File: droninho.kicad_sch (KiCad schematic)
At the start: 22 parts, among them J1 Conn_01x02_Pin, J2 M2, J3 M1, J4 M3, J5 M4, J6 I2C, J7 TXD0/RXD0, J8 I2C, Q1 SI2300, Q2 SI2300, Q3 SI2300, Q4 SI2300, U2 ESP32 Dev Kit, U4 MPU9250/6500

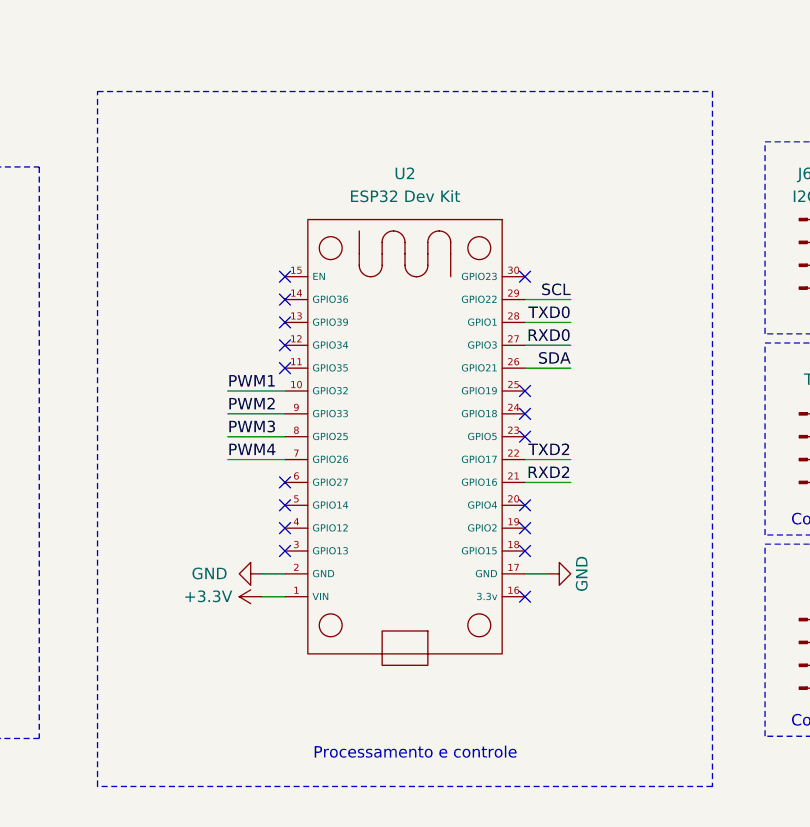
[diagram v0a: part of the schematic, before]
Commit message: Versão com WIFI de fora da placa.
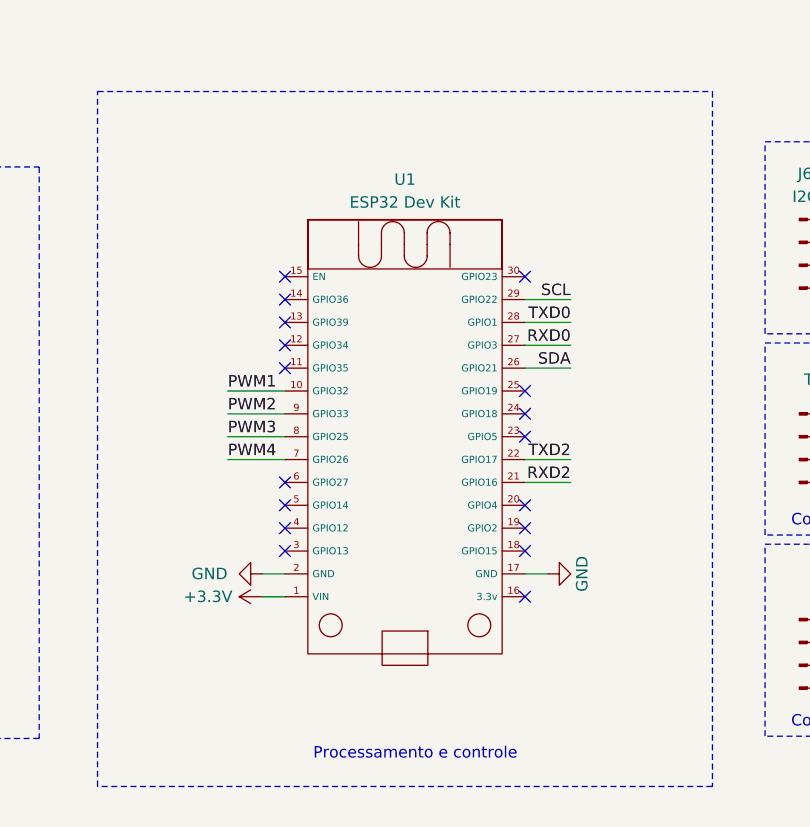
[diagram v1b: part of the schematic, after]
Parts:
- removed U2: ESP32 Dev Kit, Library:ESP32_30pin, symbol Library:ESP32_30Pin
- added U1: ESP32 Dev Kit, Library:ESP32_30pin vertical WIFI, symbol Library:ESP32_30Pin_vertical_WIFI
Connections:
- net +3.3V: now also U1.1 (VIN)
- net GND: now also U1.17 (GND), U1.2 (GND)
- net PWM1: now also U1.10 (GPIO32)
- net PWM2: now also U1.9 (GPIO33)
- net PWM3: now also U1.8 (GPIO25)
- net PWM4: now also U1.7 (GPIO26)
- net RXD0: now also U1.27 (GPIO3)
- net RXD2: now also U1.21 (GPIO16)
- net SCL: now also U1.29 (GPIO22)
- net SDA: now also U1.26 (GPIO21)
- net TXD0: now also U1.28 (GPIO1)
- net TXD2: now also U1.22 (GPIO17)
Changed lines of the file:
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@@
+	)
+	(symbol
+		(lib_id "Library:ESP32_30Pin_vertical_WIFI")
+		(at 207.01 95.885 0)
+		(unit 1)
+		(exclude_from_sim no)
+		(in_bom yes)
+		(on_board yes)
+		(dnp no)
+		(fields_autoplaced yes)
+		(property "Reference" "U1"
+			(at 206.375 70.485 0)
+			(effects
+				(font
+					(size 1.27 1.27)
+				)
+			)
+		)
+		(property "Value" "ESP32 Dev Kit"
+			(at 206.375 73.025 0)
+			(effects
+				(font
+					(size 1.27 1.27)
+				)
+			)
+		)
+		(property "Footprint" "Library:ESP32_30pin vertical WIFI"
+			(at 206.375 72.39 0)
+			(effects
+				(font
+					(size 1.27 1.27)
+					(color 194 194 0 1)
+				)
+				(hide yes)
+			)
+		)
+		(property "Datasheet" ""
+			(at 207.01 95.885 0)
+			(effects
+				(font
+					(size 1.27 1.27)
+				)
+				(hide yes)
+			)
+		)
+		(property "Description" ""
+			(at 207.01 95.885 0)
+			(effects
+				(font
+					(size 1.27 1.27)
+				)
+				(hide yes)
+			)
+		)
+		(pin "2"
+		)
+		(pin "24"
+		)
+		(pin "23"
+		)
+		(pin "6"
+		)
+		(pin "19"
+		)
+		(pin "11"
+		)
+		(pin "16"
+		)
+		(pin "14"
+		)
+		(pin "15"
+		)
+		(pin "5"
+		)
+		(pin "7"
+		)
+		(pin "10"
+		)
+		(pin "1"
+		)
+		(pin "8"
+		)
+		(pin "3"
+		)
+		(pin "28"
+		)
+		(pin "12"
+		)
+		(pin "4"
+		)
+		(pin "27"
+		)
+		(pin "13"
+		)
+		(pin "9"
+		)
+		(pin "30"
+		)
+		(pin "29"
+		)
+		(pin "26"
+		)
+		(pin "25"
+		)
+		(pin "22"
+		)
+		(pin "21"
+		)
+		(pin "20"
+		)
+		(pin "18"
+		)
+		(pin "17"
+		)
+		(instances
+			(project ""
+				(path "/50215636-8ce2-4b01-ade7-3715bffabe9d"
+					(reference "U1")
+					(unit 1)
+				)
+			)
+		)
 	)
 	(symbol
@@
 					(unit 1)
 				)
-			)
-		)
-	)
-	(symbol
-		(lib_id "Library:ESP32_30Pin")
-		(at 206.375 99.06 270)
-		(unit 1)
-		(exclude_from_sim no)
-		(in_bom yes)
-		(on_board yes)
-		(dnp no)
-		(fields_autoplaced yes)
-		(property "Reference" "U2"
-			(at 206.375 69.85 90)
-			(effects
-				(font
-					(size 1.27 1.27)
-				)
-			)
-		)
-		(property "Value" "ESP32 Dev Kit"
-			(at 206.375 72.39 90)
-			(effects
-				(font
-					(size 1.27 1.27)
-				)
-			)
-		)
-		(property "Footprint" "Library:ESP32_30pin"
-			(at 206.375 72.39 90)
-			(effects
-				(font
-					(size 1.27 1.27)
-					(color 194 194 0 1)
-				)
-				(hide yes)
-			)
-		)
-		(property "Datasheet" ""
-			(at 206.375 99.06 0)
-			(effects
-				(font
-					(size 1.27 1.27)
-				)
-				(hide yes)
-			)
-		)
-		(property "Description" ""
-			(at 206.375 99.06 0)
-			(effects
-				(font
-					(size 1.27 1.27)
-				)
-				(hide yes)
-			)
-		)
-		(pin "15"
-		)
-		(pin "14"
-		)
-		(pin "30"
-		)
-		(pin "29"
-		)
-		(pin "19"
-		)
-		(pin "7"
-		)
-		(pin "12"
-		)
-		(pin "21"
-		)
-		(pin "6"
-		)
-		(pin "9"
-		)
-		(pin "26"
-		)
-		(pin "24"
-		)
-		(pin "17"
-		)
-		(pin "5"
-		)
-		(pin "13"
-		)
-		(pin "10"
-		)
-		(pin "25"
-		)
-		(pin "23"
-		)
-		(pin "8"
-		)
-		(pin "22"
-		)
-		(pin "20"
-		)
-		(pin "28"
-		)
-		(pin "18"
-		)
-		(pin "3"
-		)
-		(pin "2"
-		)
-		(pin "11"
-		)
-		(pin "27"
-		)
-		(pin "4"
-		)
-		(pin "16"
-		)
-		(pin "1"
-		)
-		(instances
-			(project ""
-				(path "/50215636-8ce2-4b01-ade7-3715bffabe9d"
-					(reference "U2")
-					(unit 1)
-				)

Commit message: Correções em footprints e troca de lado do ESP32.
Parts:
- D1, D2, D3, D4: footprint Diode_SMD:D_SOD-110 -> Diode_SMD:D_SOD-123
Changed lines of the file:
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@@
 			)
 		)
-		(property "Footprint" "Diode_SMD:D_SOD-110"
+		(property "Footprint" "Diode_SMD:D_SOD-123"
 			(at 86.106 161.036 0)
 			(effects
@@
 			)
 		)
-		(property "Footprint" "Diode_SMD:D_SOD-110"
+		(property "Footprint" "Diode_SMD:D_SOD-123"
 			(at 86.106 116.586 0)
 			(effects
@@
 			)
 		)
-		(property "Footprint" "Diode_SMD:D_SOD-110"
+		(property "Footprint" "Diode_SMD:D_SOD-123"
 			(at 83.566 28.956 0)
 			(effects
@@
 			)
 		)
-		(property "Footprint" "Diode_SMD:D_SOD-110"
+		(property "Footprint" "Diode_SMD:D_SOD-123"
 			(at 83.566 72.136 0)
 			(effects

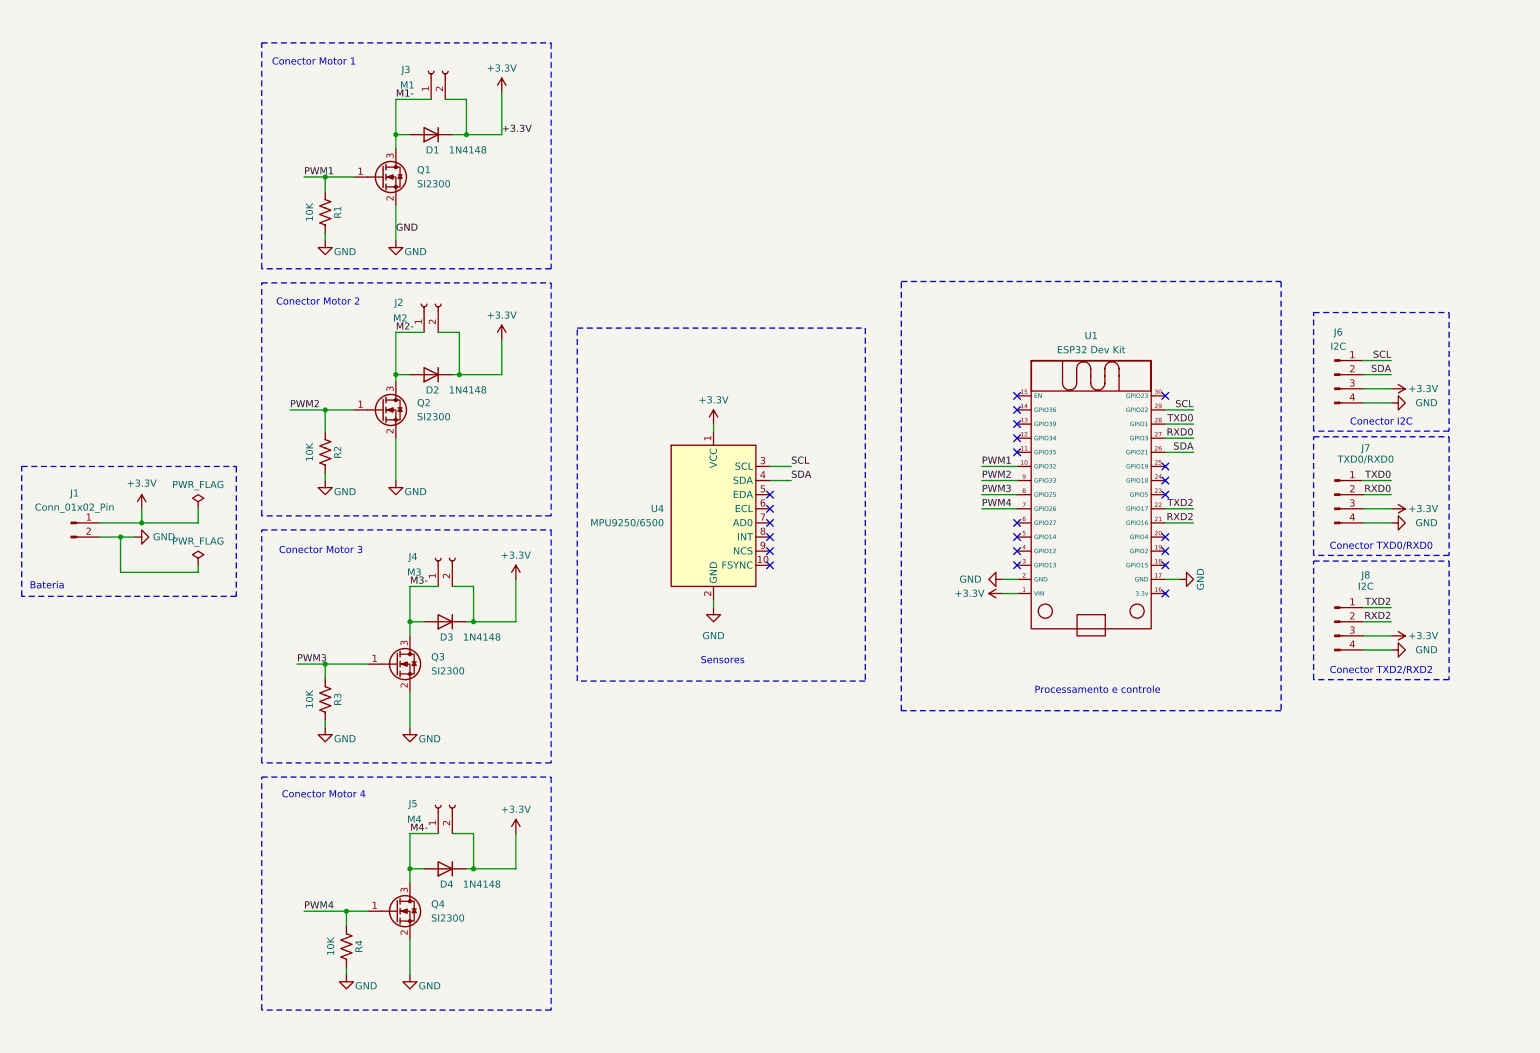
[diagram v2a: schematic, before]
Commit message: voltage regulator added
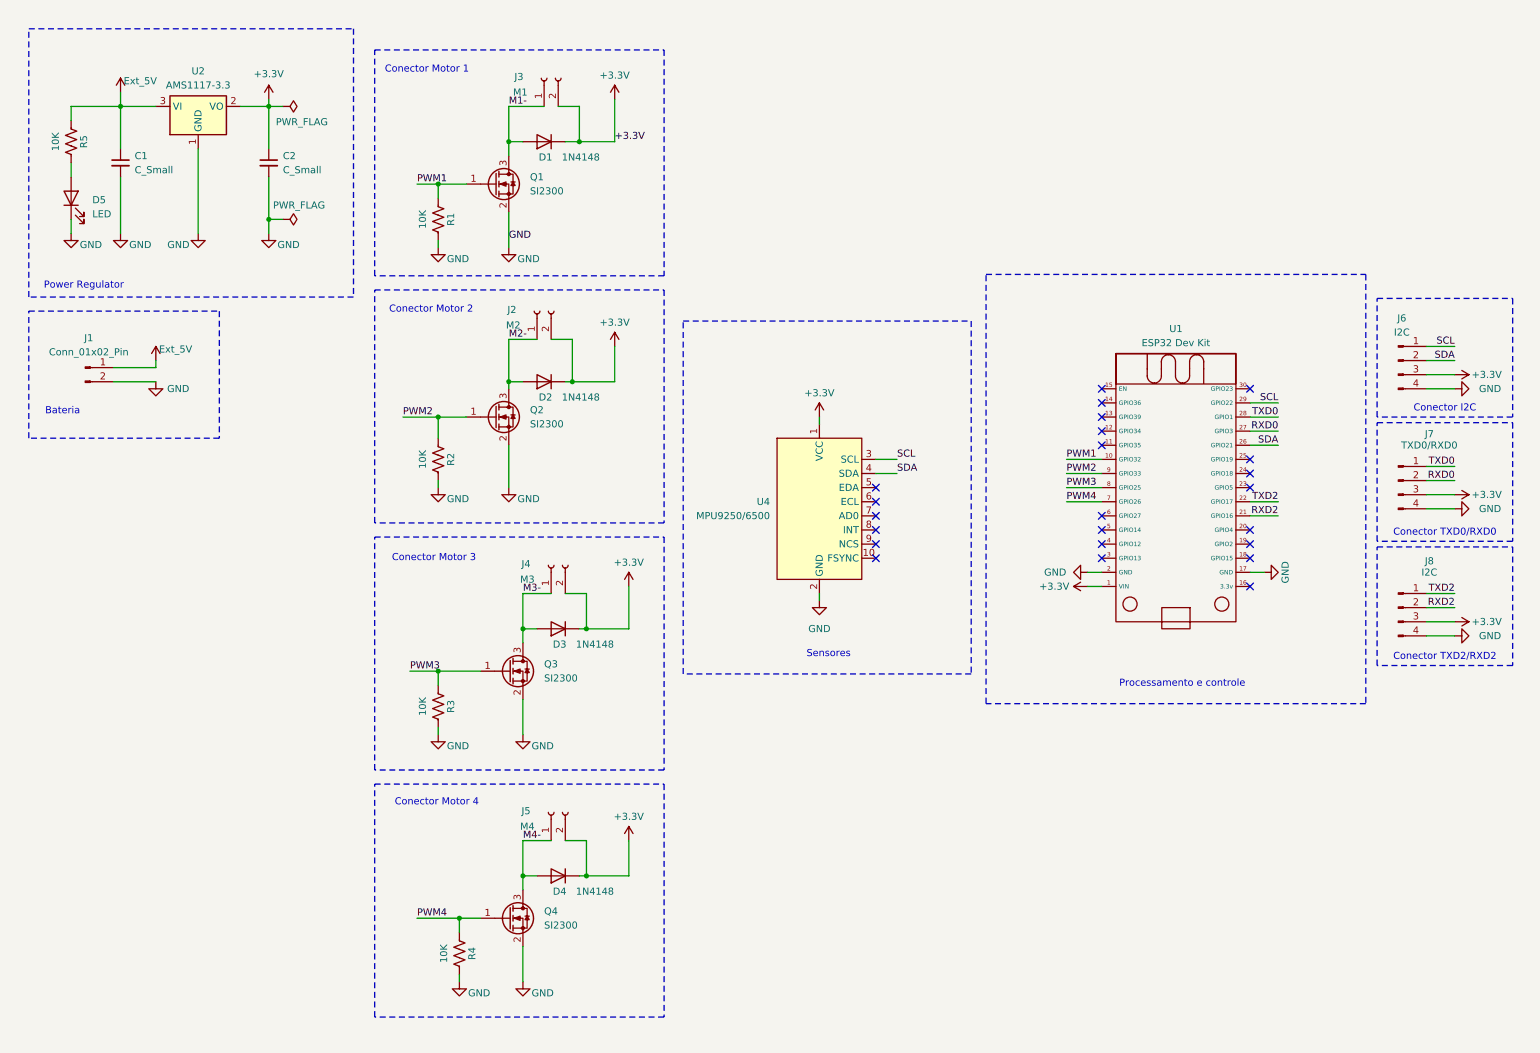
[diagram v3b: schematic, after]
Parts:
- added C1, C2: C_Small, Capacitor_SMD:C_0805_2012Metric_Pad1.18x1.45mm_HandSolder, symbol Device:C_Small
- added D5: LED, LED_SMD:LED_0805_2012Metric_Pad1.15x1.40mm_HandSolder, symbol Device:LED
- added R5: 10K, Resistor_SMD:R_0805_2012Metric_Pad1.20x1.40mm_HandSolder, symbol Device:R_US
- added U2: AMS1117-3.3, Package_TO_SOT_SMD:SOT-223-3_TabPin2, symbol Regulator_Linear:AMS1117-3.3
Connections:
- net +3.3V: now also C2.1, U2.2 (VO); no longer J1.1 (Pin_1)
- net GND: now also C1.2, C2.2, D5.1 (K), U2.1 (GND)
- new net: D5.2 (A), R5.2
- new net Ext_5V: C1.1, J1.1 (Pin_1), R5.1, U2.3 (VI)
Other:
- note added: "Power Regulator"
- moved on the sheet: D1, D2, D3, D4, J1, J2, J3, J4, J5, J6, J7, J8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

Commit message: ERC done!
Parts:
- added D2, D3, D4, D5: LED, LED_SMD:LED_0805_2012Metric_Pad1.15x1.40mm_HandSolder, symbol Device:LED
- added R2, R3, R4, R5: 10K, Resistor_SMD:R_0805_2012Metric_Pad1.20x1.40mm_HandSolder, symbol Device:R_US
- renumbered D5 to D1, D1 to D6, D2 to D7, D3 to D8, D4 to D9, R5 to R1, R1 to R6, R2 to R7, R3 to R8, R4 to R9, U2 to U1, U4 to U2, U1 to U3
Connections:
- net GND: now also D2.1 (K), D3.1 (K), D4.1 (K), D5.1 (K)
- net PWM1: now also R2.1
- net PWM2: now also R3.1
- net PWM3: now also R4.1
- net PWM4: now also R5.1
- net Ext_5V renamed BAT+
- new net: D2.2 (A), R2.2
- new net: D3.2 (A), R3.2
- new net: D4.2 (A), R4.2
- new net: D5.2 (A), R5.2
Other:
- note added: "Conector de Bateria"
- note added: "Diodos LEDS PWM"
- note removed: "Bateria"
- moved on the sheet: C1, C2, D1, D6, D7, D8, D9, J1, J2, J3, J4, J5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

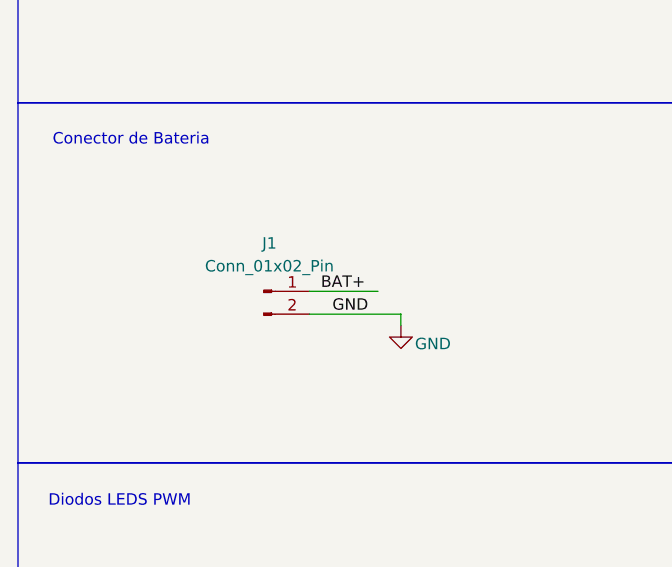
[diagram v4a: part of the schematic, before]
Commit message: Source and Battery connector added!
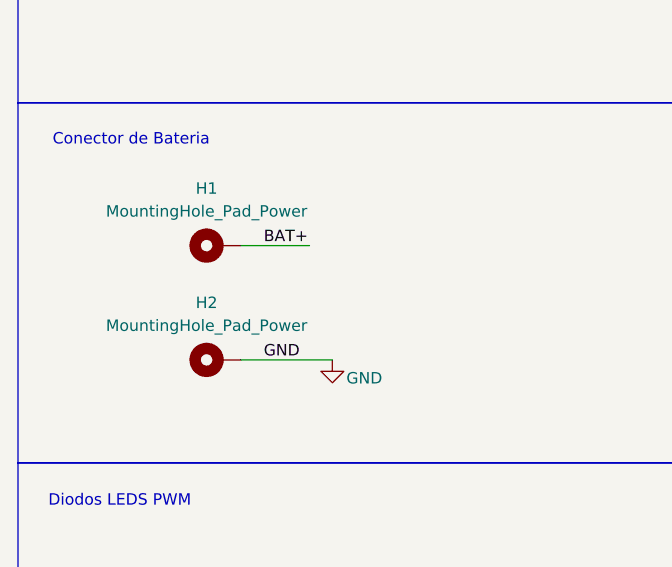
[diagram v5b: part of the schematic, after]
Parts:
- removed J1: Conn_01x02_Pin, Connector_JST:JST_EH_B2B-EH-A_1x02_P2.50mm_Vertical, symbol Connector:Conn_01x02_Pin
- added H1, H2: MountingHole_Pad_Power, MountingHole:MountingHole_2.2mm_M2_Pad_TopBottom, symbol Mechanical:MountingHole_Pad_Power
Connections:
- net BAT+: now also H1.1
- net GND: now also H2.1
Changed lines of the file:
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@@
 	(wire
 		(pts
-			(xy 54.61 99.06) (xy 54.61 100.33)
-		)
-		(stroke
-			(width 0)
-			(type default)
-		)
-	)
-	(wire
-		(pts
 			(xy 256.54 27.94) (xy 261.62 27.94)
 		)
@@
 	(wire
 		(pts
-			(xy 44.45 96.52) (xy 52.07 96.52)
+			(xy 36.83 91.44) (xy 44.45 91.44)
 		)
 		(stroke
@@
 	(wire
 		(pts
-			(xy 44.45 99.06) (xy 54.61 99.06)
+			(xy 36.83 104.14) (xy 46.99 104.14)
 		)
 		(stroke
@@
 	)
 	(label "GND"
-		(at 46.99 99.06 0)
+		(at 39.37 104.14 0)
 		(effects
 			(font
@@
 	)
 	(label "BAT+"
-		(at 45.72 96.52 0)
+		(at 39.37 91.44 0)
 		(effects
 			(font
@@
 		(length 2.54)
 		(shape round)
-		(at 52.07 96.52 270)
+		(at 44.45 91.44 270)
 		(effects
 			(font
@@
 		)
 		(property "Netclass" "Ext_5v"
-			(at 55.88 96.52 0)
+			(at 48.26 91.44 0)
 			(effects
 				(font
@@
 		)
 		(property "Component Class" ""
-			(at -26.67 29.21 0)
+			(at -34.29 24.13 0)
 			(effects
 				(font
@@
 	(symbol
 		(lib_id "power:GND")
-		(at 54.61 100.33 0)
+		(at 46.99 104.14 0)
 		(unit 1)
 		(exclude_from_sim no)
@@
 		(dnp no)
 		(property "Reference" "#PWR03"
-			(at 54.61 106.68 0)
+			(at 46.99 110.49 0)
 			(effects
 				(font
@@
 		)
 		(property "Value" "GND"
-			(at 58.166 102.362 0)
+			(at 50.546 106.172 0)
 			(effects
 				(font
@@
 		)
 		(property "Footprint" ""
-			(at 54.61 100.33 0)
+			(at 46.99 104.14 0)
 			(effects
 				(font
@@
 		)
 		(property "Datasheet" ""
-			(at 54.61 100.33 0)
+			(at 46.99 104.14 0)
 			(effects
 				(font
@@
 		)
 		(property "Description" "Power symbol creates a global label with name \"GND\" , ground"
-			(at 54.61 100.33 0)
+			(at 46.99 104.14 0)
 			(effects
 				(font
@@
 	)
 	(symbol
+		(lib_id "Mechanical:MountingHole_Pad_Power")
+		(at 34.29 91.44 90)
+		(unit 1)
+		(exclude_from_sim yes)
+		(in_bom no)
+		(on_board yes)
+		(dnp no)
+		(fields_autoplaced yes)
+		(property "Reference" "H1"
+			(at 33.02 85.09 90)
+			(effects
+				(font
+					(size 1.27 1.27)
+				)
+			)
+		)
+		(property "Value" "MountingHole_Pad_Power"
+			(at 33.02 87.63 90)
+			(effects
+				(font
+					(size 1.27 1.27)
+				)
+			)
+		)
+		(property "Footprint" "MountingHole:MountingHole_2.2mm_M2_Pad_TopBottom"
+			(at 34.29 91.44 0)
+			(effects
+				(font
+					(size 1.27 1.27)
+				)
+				(hide yes)
+			)
+		)
+		(property "Datasheet" "~"
+			(at 34.29 91.44 0)
+			(effects
+				(font
+					(size 1.27 1.27)
+				)
+				(hide yes)
+			)
+		)
+		(property "Description" "Mounting Hole with connection"
+			(at 34.29 91.44 0)
+			(effects
+				(font
+					(size 1.27 1.27)
+				)
+				(hide yes)
+			)
+		)
+		(pin "1"
+		)
+		(instances
+			(project ""
+				(path "/50215636-8ce2-4b01-ade7-3715bffabe9d"
+					(reference "H1")
+					(unit 1)
+				)
+			)
+		)
+	)
+	(symbol
 		(lib_id "power:GND")
 		(at 64.77 55.88 0)
@@
 	)
 	(symbol
-		(lib_id "Connector:Conn_01x02_Pin")
-		(at 39.37 96.52 0)
-		(unit 1)
-		(exclude_from_sim no)
-		(in_bom yes)
-		(on_board yes)
-		(dnp no)
-		(fields_autoplaced yes)
-		(property "Reference" "J1"
-			(at 40.005 91.186 0)
-			(effects
-				(font
-					(size 1.27 1.27)
-				)
-			)
-		)
-		(property "Value" "Conn_01x02_Pin"
-			(at 40.005 93.726 0)
-			(effects
-				(font
-					(size 1.27 1.27)
-				)
-			)
-		)
-		(property "Footprint" "Connector_JST:JST_EH_B2B-EH-A_1x02_P2.50mm_Vertical"
-			(at 39.37 96.52 0)
-			(effects
-				(font
-					(size 1.27 1.27)
-				)
-				(hide yes)
-			)
-		)
-		(property "Datasheet" "~"
-			(at 39.37 96.52 0)
-			(effects
-				(font
-					(size 1.27 1.27)
-				)
-				(hide yes)
-			)
-		)
-		(property "Description" "Generic connector, single row, 01x02, script generated"
-			(at 39.37 96.52 0)
-			(effects
-				(font
-					(size 1.27 1.27)
-				)
-				(hide yes)
-			)
-		)
-		(pin "2"
-		)
-		(pin "1"
-		)
-		(instances
-			(project ""
-				(path "/50215636-8ce2-4b01-ade7-3715bffabe9d"
-					(reference "J1")
-					(unit 1)
-				)
-			)
-		)
-	)
-	(symbol
 		(lib_id "power:GND")
 		(at 29.21 55.88 0)
@@
 					(unit 1)
 				)
+			)
+		)
+	)
+	(symbol
+		(lib_id "Mechanical:MountingHole_Pad_Power")
+		(at 34.29 104.14 90)
+		(unit 1)
+		(exclude_from_sim yes)
+		(in_bom no)
+		(on_board yes)
+		(dnp no)
+		(fields_autoplaced yes)
+		(property "Reference" "H2"
+			(at 33.02 97.79 90)
+			(effects
+				(font
+					(size 1.27 1.27)
+				)
+			)
+		)
+		(property "Value" "MountingHole_Pad_Power"
+			(at 33.02 100.33 90)
+			(effects
+				(font
+					(size 1.27 1.27)
+				)
+			)
+		)
+		(property "Footprint" "MountingHole:MountingHole_2.2mm_M2_Pad_TopBottom"
+			(at 34.29 104.14 0)
+			(effects
+				(font
+					(size 1.27 1.27)
+				)
+				(hide yes)
+			)
+		)
+		(property "Datasheet" "~"
+			(at 34.29 104.14 0)
+			(effects
+				(font
+					(size 1.27 1.27)
+				)
+				(hide yes)
+			)
+		)
+		(property "Description" "Mounting Hole with connection"
+			(at 34.29 104.14 0)
+			(effects
+				(font
+					(size 1.27 1.27)
+				)
+				(hide yes)
+			)
+		)
+		(pin "1"
+		)
+		(instances
+			(project "droninho"
+				(path "/50215636-8ce2-4b01-ade7-3715bffabe9d"
+					(reference "H2")
+					(unit 1)
+				)
